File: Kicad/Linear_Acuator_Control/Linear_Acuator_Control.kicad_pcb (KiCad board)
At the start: 2 copper layers, 108 x 68 mm, 31 parts, among them K1 RT42xAxx, K3 RT42xAxx, Q1 IRLB3813, Q2 IRLB3813, Q3 2N7002, Q5 2N7002, U1 ESP32-S3-WROOM

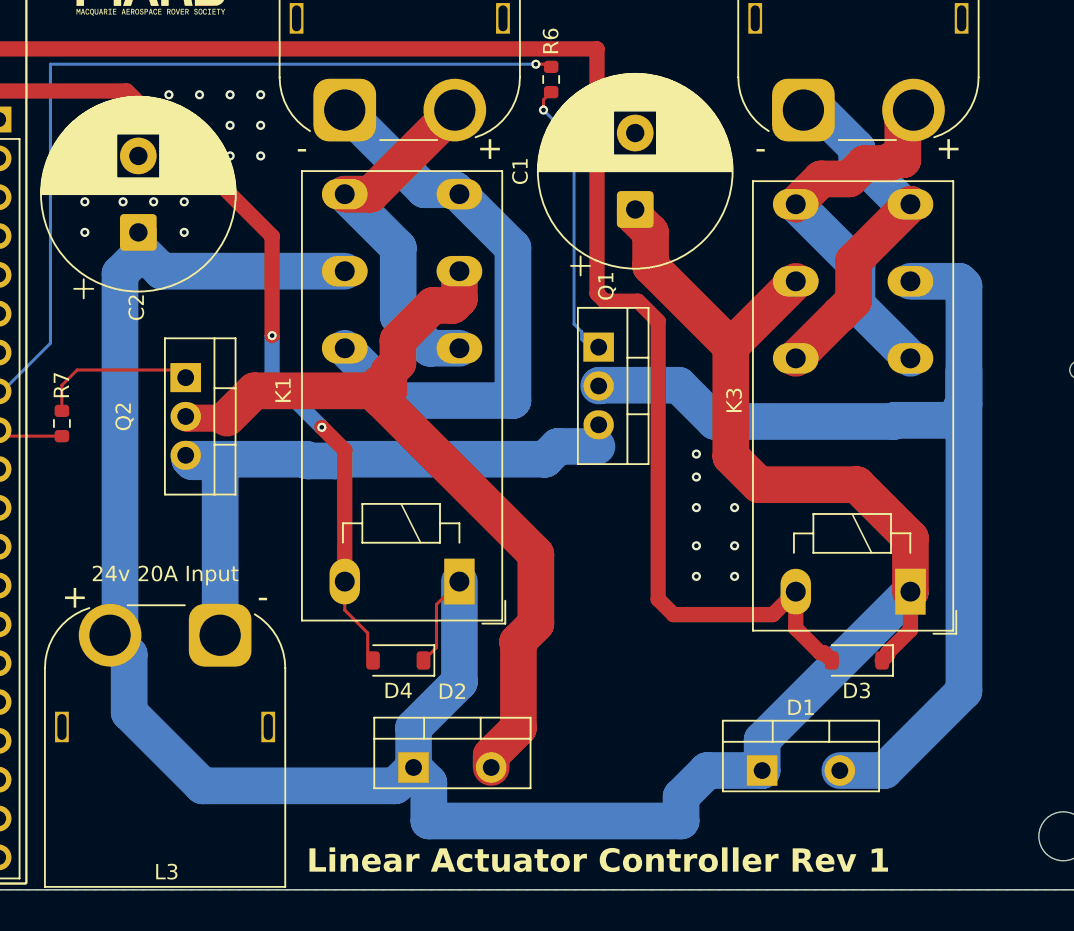
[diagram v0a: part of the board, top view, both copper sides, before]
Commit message: removing solder mask over current carrying traces, cleaning up other stuff
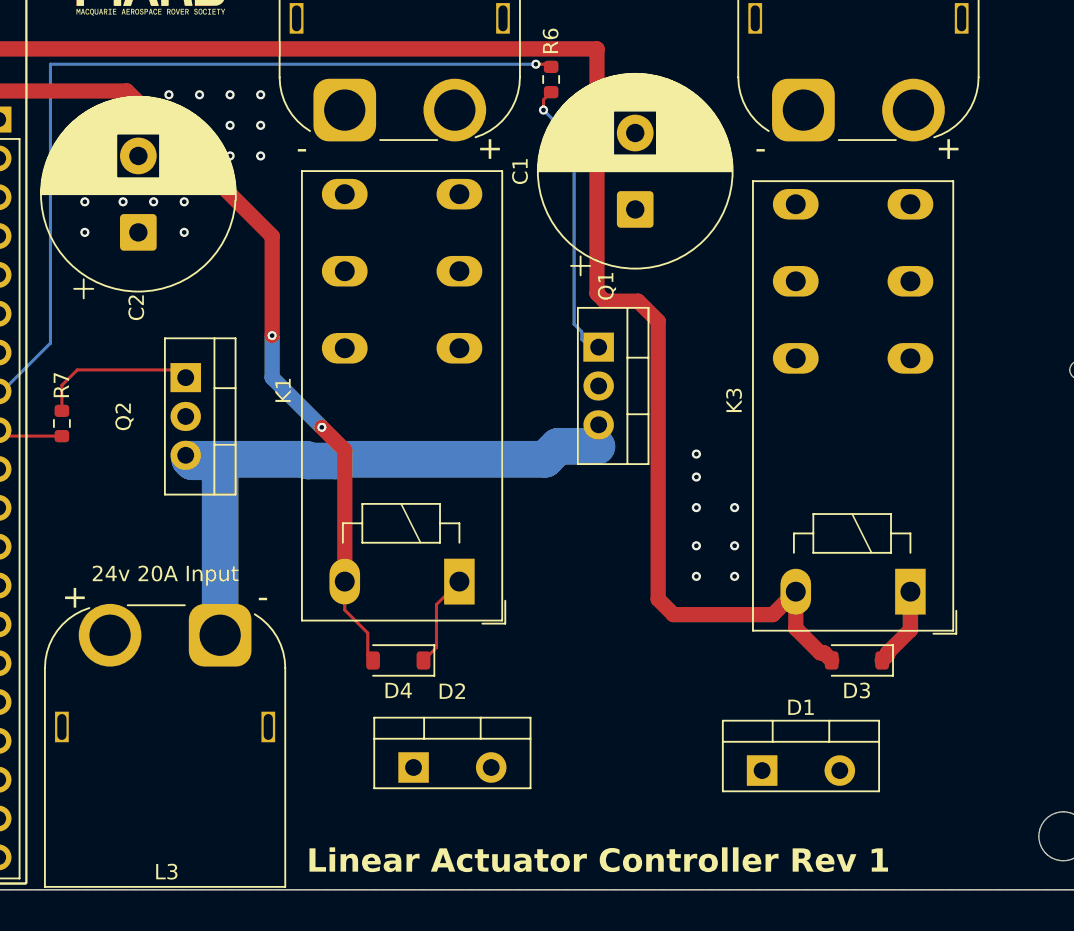
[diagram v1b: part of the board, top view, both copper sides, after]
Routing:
- net Net-(D2-A): track 55.3 -> 56.6 mm

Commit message: Fab Ready
Im pretty sure
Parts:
- C1, C2: value 1000u -> C_Elec_10x10.2; footprint Capacitor_THT:CP_Radial_D12.5mm_P5.00mm -> Capacitor_SMD:C_Elec_10x10.2
- D1, D2: value MBR745 -> D_SMB; footprint Package_TO_SOT_THT:TO-220-2_Vertical -> Diode_SMD:D_SMB
- Q1, Q2: value IRLB3813 -> SOT-23; footprint Package_TO_SOT_THT:TO-220-3_Vertical -> Package_TO_SOT_SMD:SOT-23
- moved C1 5.01 mm to (133.8, 55.5)
- moved Q1 3.35 mm to (130.2, 72.8), turned to 0 degrees
- moved D1 3.20 mm to (145.0, 97.2)
- moved D2 2.75 mm to (121.8, 97.0)
- moved C2 1.52 mm to (99.5, 61.8)
- moved Q2 1.17 mm to (105.0, 72.2), turned to 0 degrees
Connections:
- C1 pad 1: +24V -> (no net)
- C2 pad 1: +24V -> (no net)
- Q1 pad 2: L1SwitchedLow -> GND
- Q1 pad 3: GND -> L1SwitchedLow
- Q2 pad 1: Net-(Q2-G) -> (no net)
- Q2 pad 2: Net-(D2-A) -> GND
- Q2 pad 3: GND -> Net-(D2-A)
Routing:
- net GND: track 40.8 -> 0.12 mm
- net +24V: track 179.7 -> 211.3 mm, vias 0 -> 25
- net L1SwitchedLow: track 68.8 -> 74.2 mm, vias 0 -> 10
- net Net-(D2-A): track 56.6 -> 54.3 mm
- net Net-(Q1-G): track 18.7 -> 20.6 mm, vias 1 -> 2
